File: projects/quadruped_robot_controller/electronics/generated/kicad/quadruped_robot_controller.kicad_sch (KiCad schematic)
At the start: 42 parts, among them J1 24V INPUT, J11 MOTOR_IO_1, J12 MOTOR_IO_2, J13 MOTOR_IO_3, J14 MOTOR_IO_4, J15 MOTOR_IO_5, J16 MOTOR_IO_6, J17 MOTOR_IO_7, J18 MOTOR_IO_8, J19 MOTOR_IO_9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

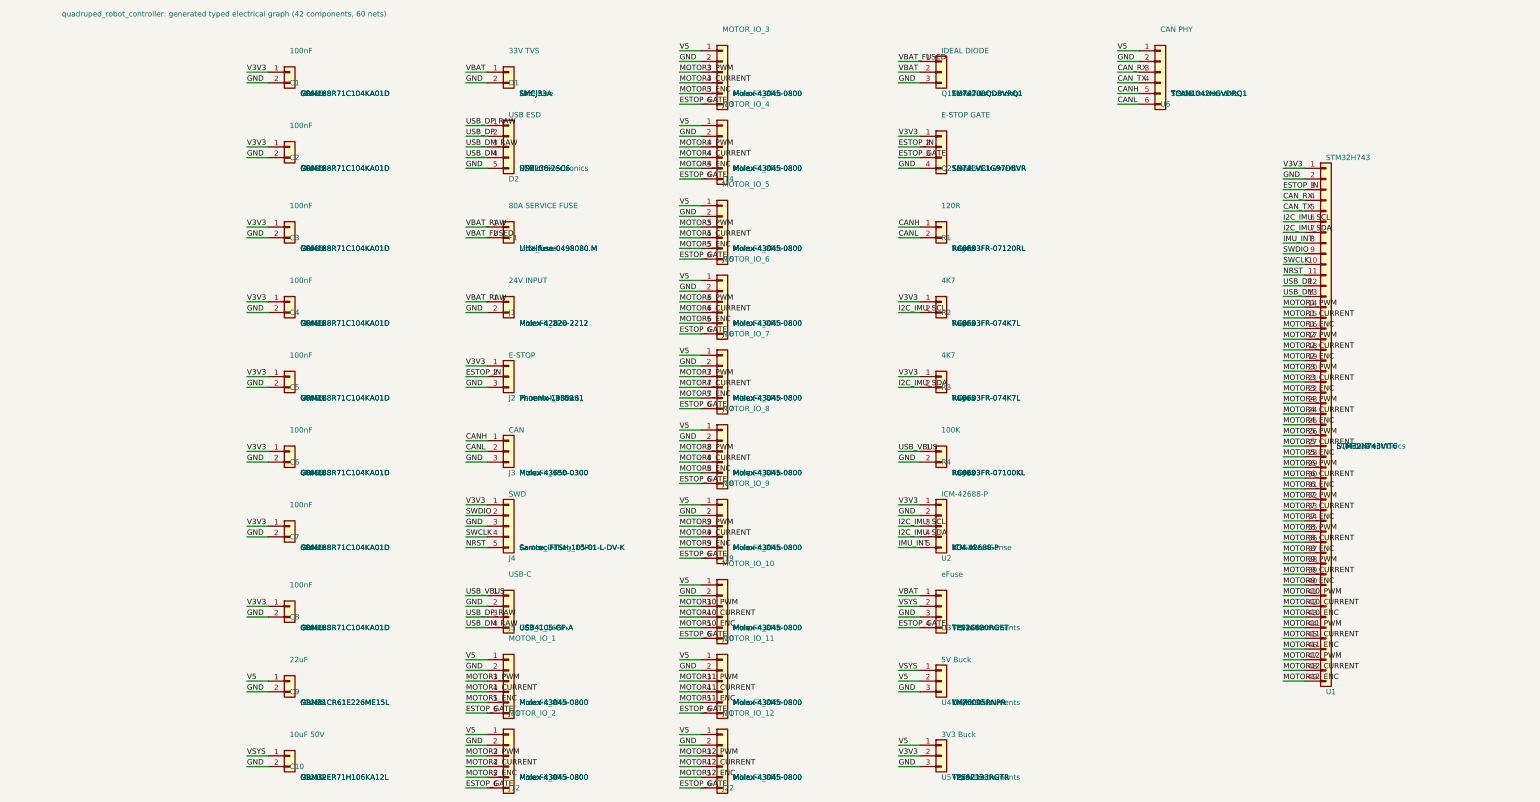
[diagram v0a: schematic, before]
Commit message: feat: component resolver, provenance tracking, and tscircuit backend gate
- Add ComponentResolver and artifact_provenance to wire real component
  data (MPN, footprint, lifecycle) into the electrical graph
- Introduce TSCircuitBackend as the first release-eligible compiled
  electronics backend; reference backend now explicitly blocks release
- Move electronics design intent from .ato source files to annotated
  .intent.md files under electronics/intent/
- Reroute BOM to electronics/generated/bom.csv; release directory is
  now exports/releases/<revision> with atomic staging via .staging/
- Add candidate bundle writing per design iteration
- Normalise MCP tool status strings and rename generate_electronics to
  hw_generate_electronics_source / hw_generate_all
- Update all tests to reflect new gate names and blocked-by-default
  release policy for the reference backend
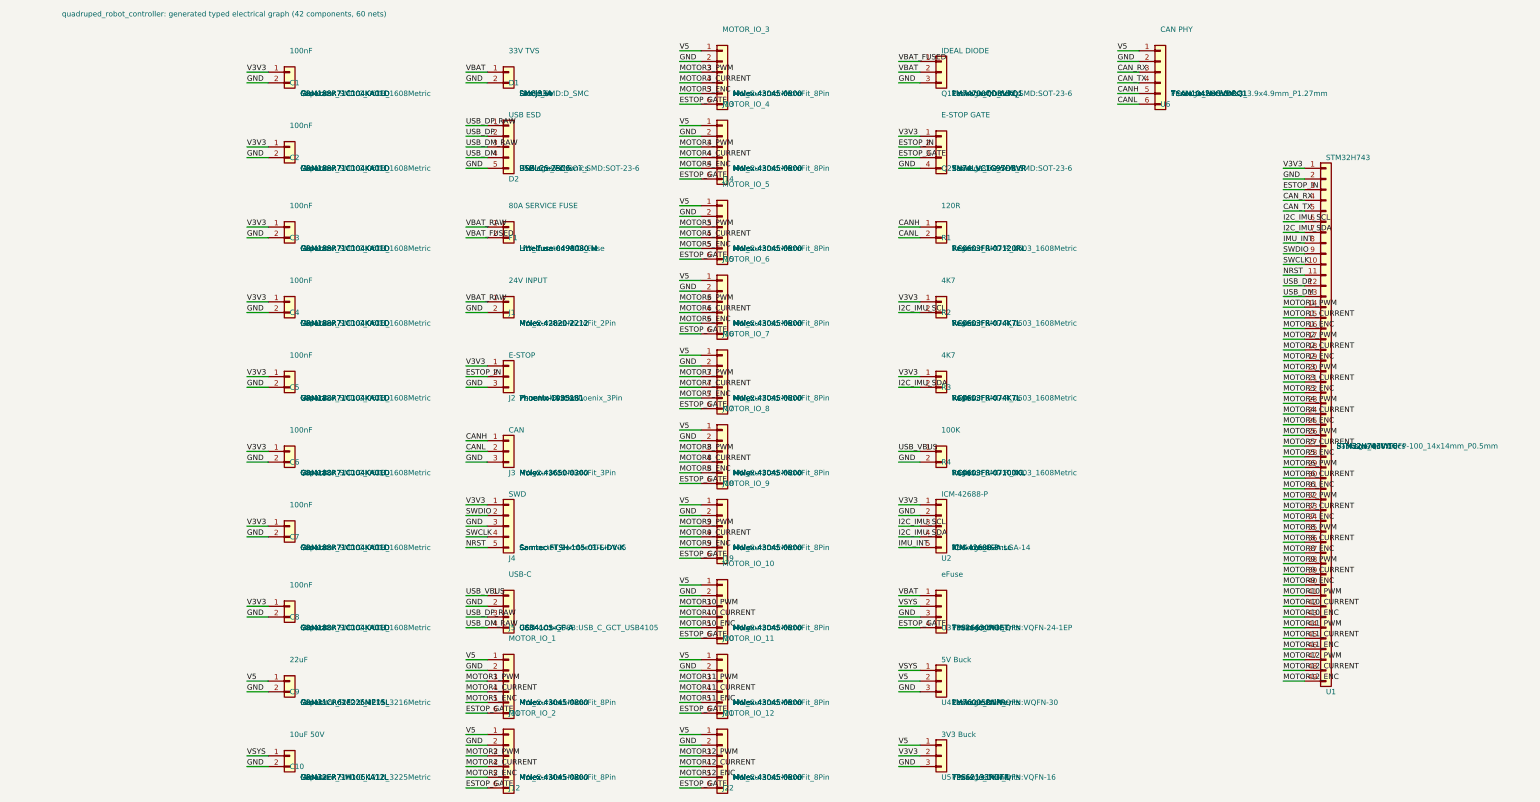
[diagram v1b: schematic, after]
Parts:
- C1, C2, C3, C4, C5, C6, C7, C8: PCB_Footprint C0603 -> Capacitor_SMD:C_0603_1608Metric
- C10: PCB_Footprint C1210 -> Capacitor_SMD:C_1210_3225Metric
- C9: PCB_Footprint C1206 -> Capacitor_SMD:C_1206_3216Metric
- D1: PCB_Footprint SMCJ -> Diode_SMD:D_SMC
- D2, Q1, Q2: PCB_Footprint SOT23-6 -> Package_TO_SOT_SMD:SOT-23-6
- F1: PCB_Footprint MIDI_Fuse -> HW_Curated:MIDI_Fuse
- J1: PCB_Footprint MicroFit_2Pin -> HW_Curated:MicroFit_2Pin
- J11, J12, J13, J14, J15, J16, J17, J18, J19, J20, J21, J22: PCB_Footprint MicroFit_8Pin -> HW_Curated:MicroFit_8Pin
- J2: PCB_Footprint Terminal_3Pin -> TerminalBlock:Phoenix_3Pin
- J3: PCB_Footprint MicroFit_3Pin -> HW_Curated:MicroFit_3Pin
- J4: PCB_Footprint Cortex_Debug_10Pin -> Connector_Samtec:FTSH-105
- J5: PCB_Footprint USB_C_16Pin -> Connector_USB:USB_C_GCT_USB4105
- R1, R2, R3, R4: PCB_Footprint R0603 -> Resistor_SMD:R_0603_1608Metric
- U1: PCB_Footprint LQFP100 -> Package_QFP:LQFP-100_14x14mm_P0.5mm
- U2: PCB_Footprint LGA14 -> Package_LGA:LGA-14
- U3: PCB_Footprint VQFN24 -> Package_DFN_QFN:VQFN-24-1EP
- U4: PCB_Footprint WQFN30 -> Package_DFN_QFN:WQFN-30
- U5: PCB_Footprint VQFN16 -> Package_DFN_QFN:VQFN-16
- U6: PCB_Footprint SOIC8 -> Package_SO:SOIC-8_3.9x4.9mm_P1.27mm
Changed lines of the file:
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@@
 			)
 		)
-		(property "PCB_Footprint" "C0603"
+		(property "PCB_Footprint" "Capacitor_SMD:C_0603_1608Metric"
 			(at 38.1 26.6699 0)
 			(effects
@@
 			)
 		)
-		(property "PCB_Footprint" "C0603"
+		(property "PCB_Footprint" "Capacitor_SMD:C_0603_1608Metric"
 			(at 38.1 44.4499 0)
 			(effects
@@
 			)
 		)
-		(property "PCB_Footprint" "C0603"
+		(property "PCB_Footprint" "Capacitor_SMD:C_0603_1608Metric"
 			(at 38.1 63.4999 0)
 			(effects
@@
 			)
 		)
-		(property "PCB_Footprint" "C0603"
+		(property "PCB_Footprint" "Capacitor_SMD:C_0603_1608Metric"
 			(at 38.1 81.2799 0)
 			(effects
@@
 			)
 		)
-		(property "PCB_Footprint" "C0603"
+		(property "PCB_Footprint" "Capacitor_SMD:C_0603_1608Metric"
 			(at 38.1 99.0599 0)
 			(effects
@@
 			)
 		)
-		(property "PCB_Footprint" "C0603"
+		(property "PCB_Footprint" "Capacitor_SMD:C_0603_1608Metric"
 			(at 38.1 116.8399 0)
 			(effects
@@
 			)
 		)
-		(property "PCB_Footprint" "C0603"
+		(property "PCB_Footprint" "Capacitor_SMD:C_0603_1608Metric"
 			(at 38.1 134.6199 0)
 			(effects
@@
 			)
 		)
-		(property "PCB_Footprint" "C0603"
+		(property "PCB_Footprint" "Capacitor_SMD:C_0603_1608Metric"
 			(at 38.1 153.6699 0)
 			(effects
@@
 			)
 		)
-		(property "PCB_Footprint" "C1206"
+		(property "PCB_Footprint" "Capacitor_SMD:C_1206_3216Metric"
 			(at 38.1 171.4499 0)
 			(effects
@@
 			)
 		)
-		(property "PCB_Footprint" "C1210"
+		(property "PCB_Footprint" "Capacitor_SMD:C_1210_3225Metric"
 			(at 38.1 189.2299 0)
 			(effects
@@
 			)
 		)
-		(property "PCB_Footprint" "SMCJ"
+		(property "PCB_Footprint" "Diode_SMD:D_SMC"
 			(at 90.17 26.6699 0)
 			(effects
@@
 			)
 		)
-		(property "PCB_Footprint" "SOT23-6"
+		(property "PCB_Footprint" "Package_TO_SOT_SMD:SOT-23-6"
 			(at 90.17 44.4499 0)
 			(effects
@@
 			)
 		)
-		(property "PCB_Footprint" "MIDI_Fuse"
+		(property "PCB_Footprint" "HW_Curated:MIDI_Fuse"
 			(at 90.17 63.4999 0)
 			(effects
@@
 			)
 		)
-		(property "PCB_Footprint" "MicroFit_2Pin"
+		(property "PCB_Footprint" "HW_Curated:MicroFit_2Pin"
 			(at 90.17 81.2799 0)
 			(effects
@@
 			)
 		)
-		(property "PCB_Footprint" "Terminal_3Pin"
+		(property "PCB_Footprint" "TerminalBlock:Phoenix_3Pin"
 			(at 90.17 99.0599 0)
 			(effects
@@
 			)
 		)
-		(property "PCB_Footprint" "MicroFit_3Pin"
+		(property "PCB_Footprint" "HW_Curated:MicroFit_3Pin"
 			(at 90.17 116.8399 0)
 			(effects
@@
 			)
 		)
-		(property "PCB_Footprint" "Cortex_Debug_10Pin"
+		(property "PCB_Footprint" "Connector_Samtec:FTSH-105"
 			(at 90.17 134.6199 0)
 			(effects
@@
 			)
 		)
-		(property "PCB_Footprint" "USB_C_16Pin"
+		(property "PCB_Footprint" "Connector_USB:USB_C_GCT_USB4105"
 			(at 90.17 153.6699 0)
 			(effects
@@
 			)
 		)
-		(property "PCB_Footprint" "MicroFit_8Pin"
+		(property "PCB_Footprint" "HW_Curated:MicroFit_8Pin"
 			(at 90.17 171.4499 0)
 			(effects
@@
 			)
 		)
-		(property "PCB_Footprint" "MicroFit_8Pin"
+		(property "PCB_Footprint" "HW_Curated:MicroFit_8Pin"
 			(at 90.17 189.2299 0)
 			(effects
@@
 			)
 		)
-		(property "PCB_Footprint" "MicroFit_8Pin"
+		(property "PCB_Footprint" "HW_Curated:MicroFit_8Pin"
 			(at 140.97 26.6699 0)
 			(effects
@@
 			)
 		)
-		(property "PCB_Footprint" "MicroFit_8Pin"
+		(property "PCB_Footprint" "HW_Curated:MicroFit_8Pin"
 			(at 140.97 44.4499 0)
 			(effects
@@
 			)
 		)
-		(property "PCB_Footprint" "MicroFit_8Pin"
+		(property "PCB_Footprint" "HW_Curated:MicroFit_8Pin"
 			(at 140.97 63.4999 0)
 			(effects
@@
 			)
 		)
-		(property "PCB_Footprint" "MicroFit_8Pin"
+		(property "PCB_Footprint" "HW_Curated:MicroFit_8Pin"
 			(at 140.97 81.2799 0)
 			(effects
@@
 			)
 		)
-		(property "PCB_Footprint" "MicroFit_8Pin"
+		(property "PCB_Footprint" "HW_Curated:MicroFit_8Pin"
 			(at 140.97 99.0599 0)
 			(effects
@@
 			)
 		)
-		(property "PCB_Footprint" "MicroFit_8Pin"
+		(property "PCB_Footprint" "HW_Curated:MicroFit_8Pin"
 			(at 140.97 116.8399 0)
 			(effects
@@
 			)
 		)
-		(property "PCB_Footprint" "MicroFit_8Pin"
+		(property "PCB_Footprint" "HW_Curated:MicroFit_8Pin"
 			(at 140.97 134.6199 0)
 			(effects
@@
 			)
 		)
-		(property "PCB_Footprint" "MicroFit_8Pin"
+		(property "PCB_Footprint" "HW_Curated:MicroFit_8Pin"
 			(at 140.97 153.6699 0)
 			(effects
@@
 			)
 		)
-		(property "PCB_Footprint" "MicroFit_8Pin"
+		(property "PCB_Footprint" "HW_Curated:MicroFit_8Pin"
 			(at 140.97 171.4499 0)
 			(effects
@@
 			)
 		)
-		(property "PCB_Footprint" "MicroFit_8Pin"
+		(property "PCB_Footprint" "HW_Curated:MicroFit_8Pin"
 			(at 140.97 189.2299 0)
 			(effects
@@
 			)
 		)
-		(property "PCB_Footprint" "SOT23-6"
+		(property "PCB_Footprint" "Package_TO_SOT_SMD:SOT-23-6"
 			(at 193.04 26.6699 0)
 			(effects
@@
 			)
 		)
-		(property "PCB_Footprint" "SOT23-6"
+		(property "PCB_Footprint" "Package_TO_SOT_SMD:SOT-23-6"
 			(at 193.04 44.4499 0)
 			(effects
@@
 			)
 		)
-		(property "PCB_Footprint" "R0603"
+		(property "PCB_Footprint" "Resistor_SMD:R_0603_1608Metric"
 			(at 193.04 63.4999 0)
 			(effects
@@
 			)
 		)
-		(property "PCB_Footprint" "R0603"
+		(property "PCB_Footprint" "Resistor_SMD:R_0603_1608Metric"
 			(at 193.04 81.2799 0)
 			(effects
@@
 			)
 		)
-		(property "PCB_Footprint" "R0603"
+		(property "PCB_Footprint" "Resistor_SMD:R_0603_1608Metric"
 			(at 193.04 99.0599 0)
 			(effects
@@
 			)
 		)
-		(property "PCB_Footprint" "R0603"
+		(property "PCB_Footprint" "Resistor_SMD:R_0603_1608Metric"
 			(at 193.04 116.8399 0)
 			(effects
@@
 			)
 		)
-		(property "PCB_Footprint" "LQFP100"
+		(property "PCB_Footprint" "Package_QFP:LQFP-100_14x14mm_P0.5mm"
 			(at 284.48 110.4899 0)
 			(effects
@@
 			)
 		)
-		(property "PCB_Footprint" "LGA14"
+		(property "PCB_Footprint" "Package_LGA:LGA-14"
 			(at 193.04 134.6199 0)
 			(effects
@@
 			)
 		)
-		(property "PCB_Footprint" "VQFN24"
+		(property "PCB_Footprint" "Package_DFN_QFN:VQFN-24-1EP"
 			(at 193.04 153.6699 0)
 			(effects
@@
 			)
 		)
-		(property "PCB_Footprint" "WQFN30"
+		(property "PCB_Footprint" "Package_DFN_QFN:WQFN-30"
 			(at 193.04 171.4499 0)
 			(effects
@@
 			)
 		)
-		(property "PCB_Footprint" "VQFN16"
+		(property "PCB_Footprint" "Package_DFN_QFN:VQFN-16"
 			(at 193.04 189.2299 0)
 			(effects
@@
 			)
 		)
-		(property "PCB_Footprint" "SOIC8"
+		(property "PCB_Footprint" "Package_SO:SOIC-8_3.9x4.9mm_P1.27mm"
 			(at 245.11 26.6699 0)
 			(effects
